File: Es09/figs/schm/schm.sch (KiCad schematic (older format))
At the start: 4 parts

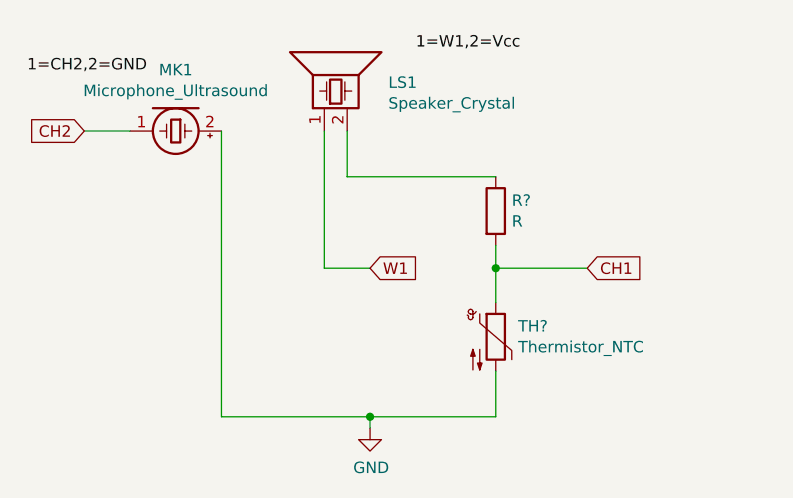
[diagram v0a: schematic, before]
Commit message: Es09: fit e misure d/t
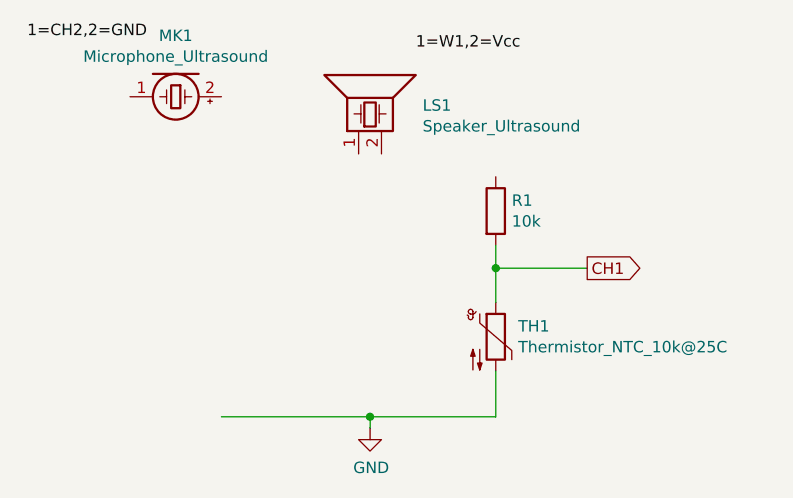
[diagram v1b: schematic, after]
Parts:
- removed LS1: Speaker_Crystal, symbol Device:Speaker_Crystal
- added LS1: Speaker_Ultrasound, symbol Device:Speaker_Ultrasound
- R1: renamed from R?; value R -> 10k
- TH1: renamed from TH?; value Thermistor_NTC -> Thermistor_NTC_10k@25C
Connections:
- net labels removed: CH2, W1
- wire segments 13 -> 7
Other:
- moved on the sheet: MK1
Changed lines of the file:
@@
 L Device:Microphone_Ultrasound MK1
 U 1 1 62090EE7
-P 2450 1550
-F 0 "MK1" V 2183 1550 50  0000 C CNN
-F 1 "Microphone_Ultrasound" V 2274 1550 50  0000 C CNN
-F 2 "" V 2500 1480 50  0001 L CNN
-F 3 "~" V 2450 1650 50  0001 C CNN
-	1    2450 1550
+P 2450 1400
+F 0 "MK1" V 2183 1400 50  0000 C CNN
+F 1 "Microphone_Ultrasound" V 2274 1400 50  0000 C CNN
+F 2 "" V 2500 1330 50  0001 L CNN
+F 3 "~" V 2450 1500 50  0001 C CNN
+	1    2450 1400
 	0    1    1    0
 $EndComp
 $Comp
-L Device:Speaker_Crystal LS1
-U 1 1 6208F16A
-P 3100 1350
-F 0 "LS1" V 3112 1070 50  0000 R CNN
-F 1 "Speaker_Crystal" V 3021 1070 50  0000 R CNN
-F 2 "" H 3065 1300 50  0001 C CNN
-F 3 "~" H 3065 1300 50  0001 C CNN
-	1    3100 1350
-	0    -1   -1   0
-$EndComp
-$Comp
-L Device:R R?
+L Device:R R1
 U 1 1 620994D0
 P 3850 1900
-F 0 "R?" H 3920 1946 50  0000 L CNN
-F 1 "R" H 3920 1855 50  0000 L CNN
+F 0 "R1" H 3920 1946 50  0000 L CNN
+F 1 "10k" H 3920 1855 50  0000 L CNN
 F 2 "" V 3780 1900 50  0001 C CNN
 F 3 "~" H 3850 1900 50  0001 C CNN
@@
 $EndComp
 $Comp
-L Device:Thermistor_NTC TH?
+L Device:Thermistor_NTC TH1
 U 1 1 62099EA6
 P 3850 2450
-F 0 "TH?" H 3948 2496 50  0000 L CNN
-F 1 "Thermistor_NTC" H 3948 2405 50  0000 L CNN
+F 0 "TH1" H 3948 2496 50  0000 L CNN
+F 1 "Thermistor_NTC_10k@25C" H 3948 2405 50  0000 L CNN
 F 2 "" H 3850 2500 50  0001 C CNN
 F 3 "~" H 3850 2500 50  0001 C CNN
@@
 Text Label 3500 1200 0    50   ~ 0
 1=W1,2=Vcc
-Text Label 1800 1300 0    50   ~ 0
+Text Label 1800 1150 0    50   ~ 0
 1=CH2,2=GND
-Text GLabel 4250 2150 2    50   Input ~ 0
+Text GLabel 4250 2150 2    50   Output ~ 0
 CH1
 Wire Wire Line
@@
 Wire Wire Line
 	3850 2150 3850 2300
-Wire Wire Line
-	3200 1550 3200 1750
-Wire Wire Line
-	3200 1750 3850 1750
-Wire Wire Line
-	2650 1550 2650 2800
 Wire Wire Line
 	2650 2800 3300 2800
@@
 Wire Wire Line
 	3300 2800 3850 2800
-Text GLabel 2050 1550 0    50   Input ~ 0
-CH2
-Wire Wire Line
-	2050 1550 2250 1550
-Text GLabel 3300 2150 2    50   Input ~ 0
-W1
-Wire Wire Line
-	3100 1550 3100 2150
-Wire Wire Line
-	3100 2150 3300 2150
+$Comp
+L Device:Speaker_Ultrasound LS1
+U 1 1 620E3EA8
+P 3250 1450
+F 0 "LS1" V 3262 1170 50  0000 R CNN
+F 1 "Speaker_Ultrasound" V 3171 1170 50  0000 R CNN
+F 2 "" H 3215 1400 50  0001 C CNN
+F 3 "~" H 3215 1400 50  0001 C CNN
+	1    3250 1450
+	0    -1   -1   0
+$EndComp
 $EndSCHEMATC
